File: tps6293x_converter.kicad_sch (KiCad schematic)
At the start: 11 parts, among them U1 TPS62933

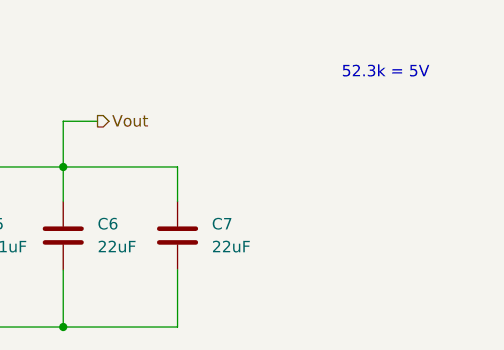
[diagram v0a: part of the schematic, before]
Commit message: sch: change undervoltage resistor value
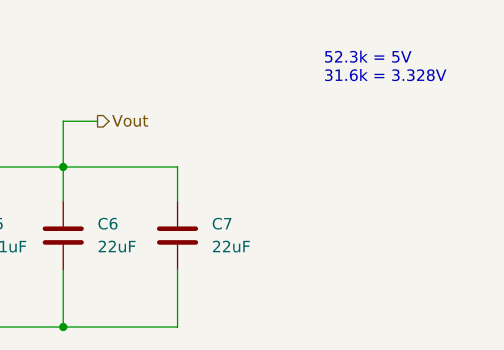
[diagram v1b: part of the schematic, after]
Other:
- note added: "52.3k = 5V 31.6k = 3.328V"
- note removed: "52.3k = 5V"
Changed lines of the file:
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@@
 		)
 	)
-	(text "52.3k = 5V"
+	(text "52.3k = 5V\n31.6k = 3.328V"
 		(exclude_from_sim no)
-		(at 199.644 22.606 0)
+		(at 192.786 22.098 0)
 		(effects
 			(font
 				(size 1.27 1.27)
 			)
+			(justify left)
 		)
 	)

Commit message: Add clarity to the choice resistors
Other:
- note added: "Vchoice 52.3k = 5V 31.6k = 3.328V"
- note removed: "52.3k = 5V 31.6k = 3.328V"
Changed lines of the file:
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@@
 		)
 	)
-	(text "52.3k = 5V\n31.6k = 3.328V"
+	(text "Vchoice\n\n52.3k = 5V\n31.6k = 3.328V"
 		(exclude_from_sim no)
 		(at 192.786 22.098 0)
